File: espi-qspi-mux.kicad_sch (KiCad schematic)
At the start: 0 parts

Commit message: [#81876] Update date, Regroup OSM L block to make it interchangeable
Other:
- title: (none) -> BMC Reference Carrier Board
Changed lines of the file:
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@@
 	(generator_version "9.0")
 	(paper "A3")
+	(title_block
+		(title "BMC Reference Carrier Board")
+		(date "2025-08-14")
+		(rev "1.0.0")
+	)
 	(hierarchical_label "QSPI{QSPI}"
 		(shape bidirectional)

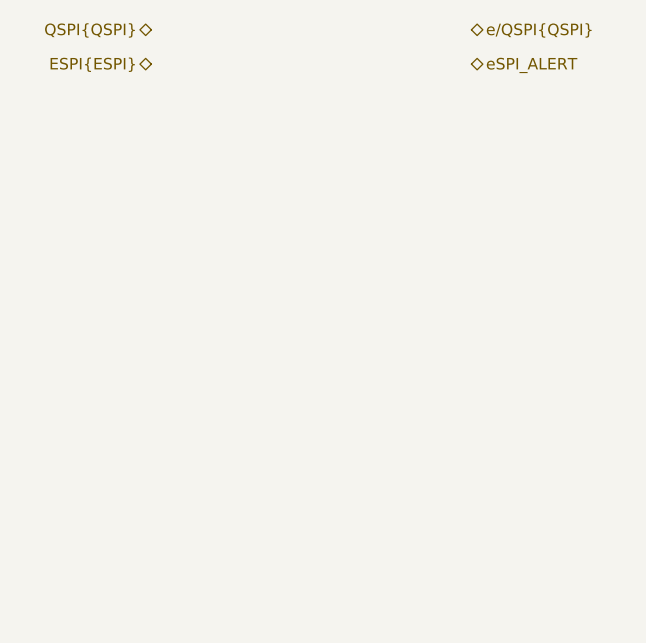
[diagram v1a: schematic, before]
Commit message: [#82233] Add eSPI/QSPI and TPM mux
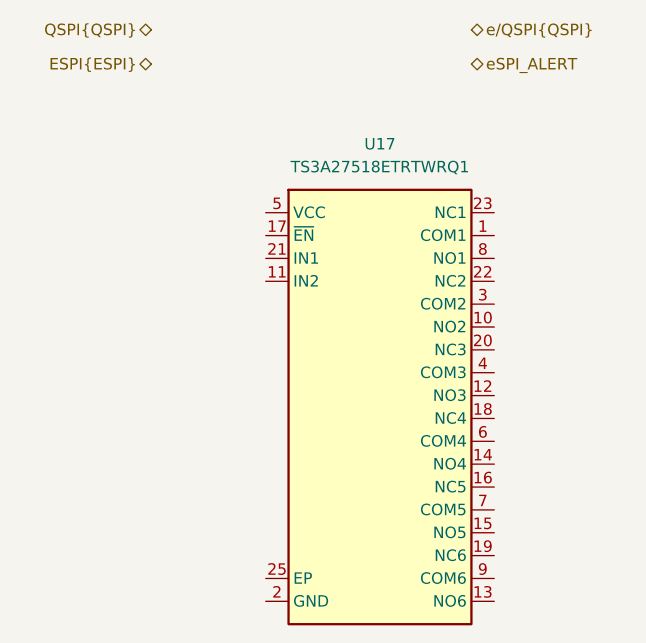
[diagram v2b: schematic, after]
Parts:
- added U17: TS3A27518E_QFN, antmicro-footprints:QFN-24-1EP_4x4mm_P0.5mm_EP2.6x2.6mm, symbol antmicroInterfaceAnalogSwitchesMultiplexersDemultiplexers:TS3A27518E_QFN
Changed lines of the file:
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@@
+		)
+	)
+	(symbol
+		(lib_id "antmicroInterfaceAnalogSwitchesMultiplexersDemultiplexers:TS3A27518E_QFN")
+		(at 153.67 149.86 0)
+		(unit 1)
+		(exclude_from_sim no)
+		(in_bom yes)
+		(on_board yes)
+		(dnp no)
+		(fields_autoplaced yes)
+		(property "Reference" "U17"
+			(at 166.37 142.24 0)
+			(effects
+				(font
+					(size 1.27 1.27)
+					(thickness 0.15)
+				)
+			)
+		)
+		(property "Value" "TS3A27518E_QFN"
+			(at 193.04 154.94 0)
+			(effects
+				(font
+					(size 1.27 1.27)
+					(thickness 0.15)
+				)
+				(justify left bottom)
+				(hide yes)
+			)
+		)
+		(property "Footprint" "antmicro-footprints:QFN-24-1EP_4x4mm_P0.5mm_EP2.6x2.6mm"
+			(at 193.04 157.48 0)
+			(effects
+				(font
+					(size 1.27 1.27)
+					(thickness 0.15)
+				)
+				(justify left bottom)
+				(hide yes)
+			)
+		)
+		(property "Datasheet" "https://www.ti.com/lit/ds/symlink/ts3a27518e-q1.pdf?HQS=dis-mous-null-mousermode-dsf-pf-null-wwe&ts=1685014732392&ref_url=https%253A%252F%252Fwww.mouser.com%252F"
+			(at 193.04 160.02 0)
+			(effects
+				(font
+					(size 1.27 1.27)
+					(thickness 0.15)
+				)
+				(justify left bottom)
+				(hide yes)
+			)
+		)
+		(property "Description" "Interface analog switch/multiplexer/demultiplexer"
+			(at 153.67 149.86 0)
+			(effects
+				(font
+					(size 1.27 1.27)
+				)
+				(hide yes)
+			)
+		)
+		(property "MPN" "TS3A27518ETRTWRQ1"
+			(at 166.37 144.78 0)
+			(effects
+				(font
+					(size 1.27 1.27)
+					(thickness 0.15)
+				)
+			)
+		)
+		(property "Manufacturer" "Texas Instruments"
+			(at 193.04 165.1 0)
+			(effects
+				(font
+					(size 1.27 1.27)
+					(thickness 0.15)
+				)
+				(justify left bottom)
+				(hide yes)
+			)
+		)
+		(property "Author" "Antmicro"
+			(at 193.04 167.64 0)
+			(effects
+				(font
+					(size 1.27 1.27)
+					(thickness 0.15)
+				)
+				(justify left bottom)
+				(hide yes)
+			)
+		)
+		(property "License" "Apache-2.0"
+			(at 193.04 170.18 0)
+			(effects
+				(font
+					(size 1.27 1.27)
+					(thickness 0.15)
+				)
+				(justify left bottom)
+				(hide yes)
+			)
+		)
+		(pin "4"
+		)
+		(pin "1"
+		)
+		(pin "7"
+		)
+		(pin "16"
+		)
+		(pin "24"
+		)
+		(pin "25"
+		)
+		(pin "13"
+		)
+		(pin "9"
+		)
+		(pin "18"
+		)
+		(pin "6"
+		)
+		(pin "8"
+		)
+		(pin "20"
+		)
+		(pin "10"
+		)
+		(pin "23"
+		)
+		(pin "3"
+		)
+		(pin "14"
+		)
+		(pin "12"
+		)
+		(pin "15"
+		)
+		(pin "21"
+		)
+		(pin "11"
+		)
+		(pin "5"
+		)
+		(pin "22"
+		)
+		(pin "2"
+		)
+		(pin "17"
+		)
+		(pin "19"
+		)
+		(instances
+			(project ""
+				(path "/5f636c45-3c15-4731-8931-4625e0dab7e4/e532ae7c-55b4-427b-a317-9e407e1b3e94"
+					(reference "U17")
+					(unit 1)
+				)
+			)
 		)
 	)

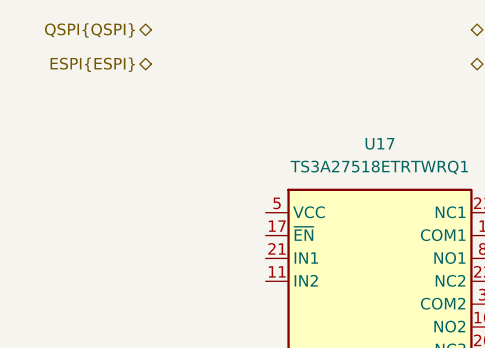
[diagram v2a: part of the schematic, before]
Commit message: [#82323] ESPI -> eSPI
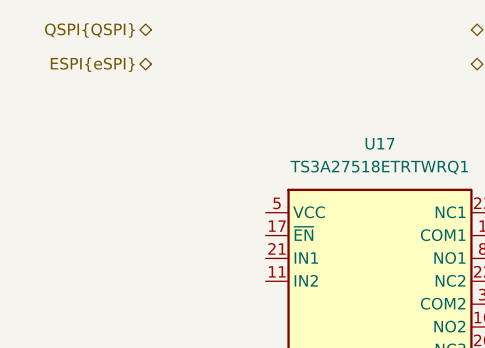
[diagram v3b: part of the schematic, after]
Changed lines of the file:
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@@
 		)
 	)
-	(hierarchical_label "ESPI{ESPI}"
+	(hierarchical_label "ESPI{eSPI}"
 		(shape bidirectional)
 		(at 140.97 133.35 180)

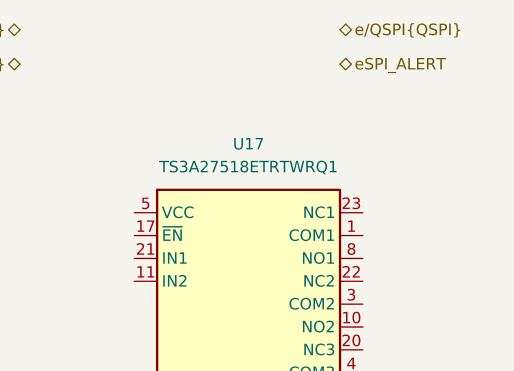
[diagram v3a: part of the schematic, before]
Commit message: [#82323] Connect OSM signals
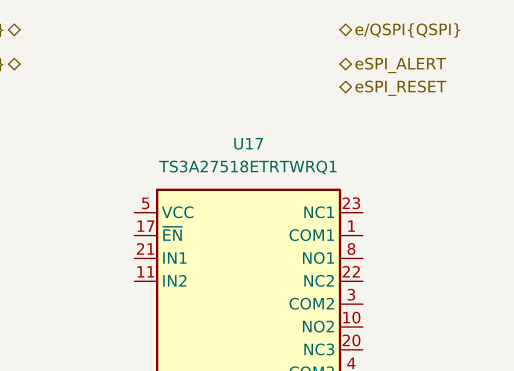
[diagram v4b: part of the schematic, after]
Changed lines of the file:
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@@
+		)
+	)
+	(hierarchical_label "eSPI_RESET"
+		(shape bidirectional)
+		(at 176.53 135.89 0)
+		(effects
+			(font
+				(size 1.27 1.27)
+			)
+			(justify left)
 		)
 	)

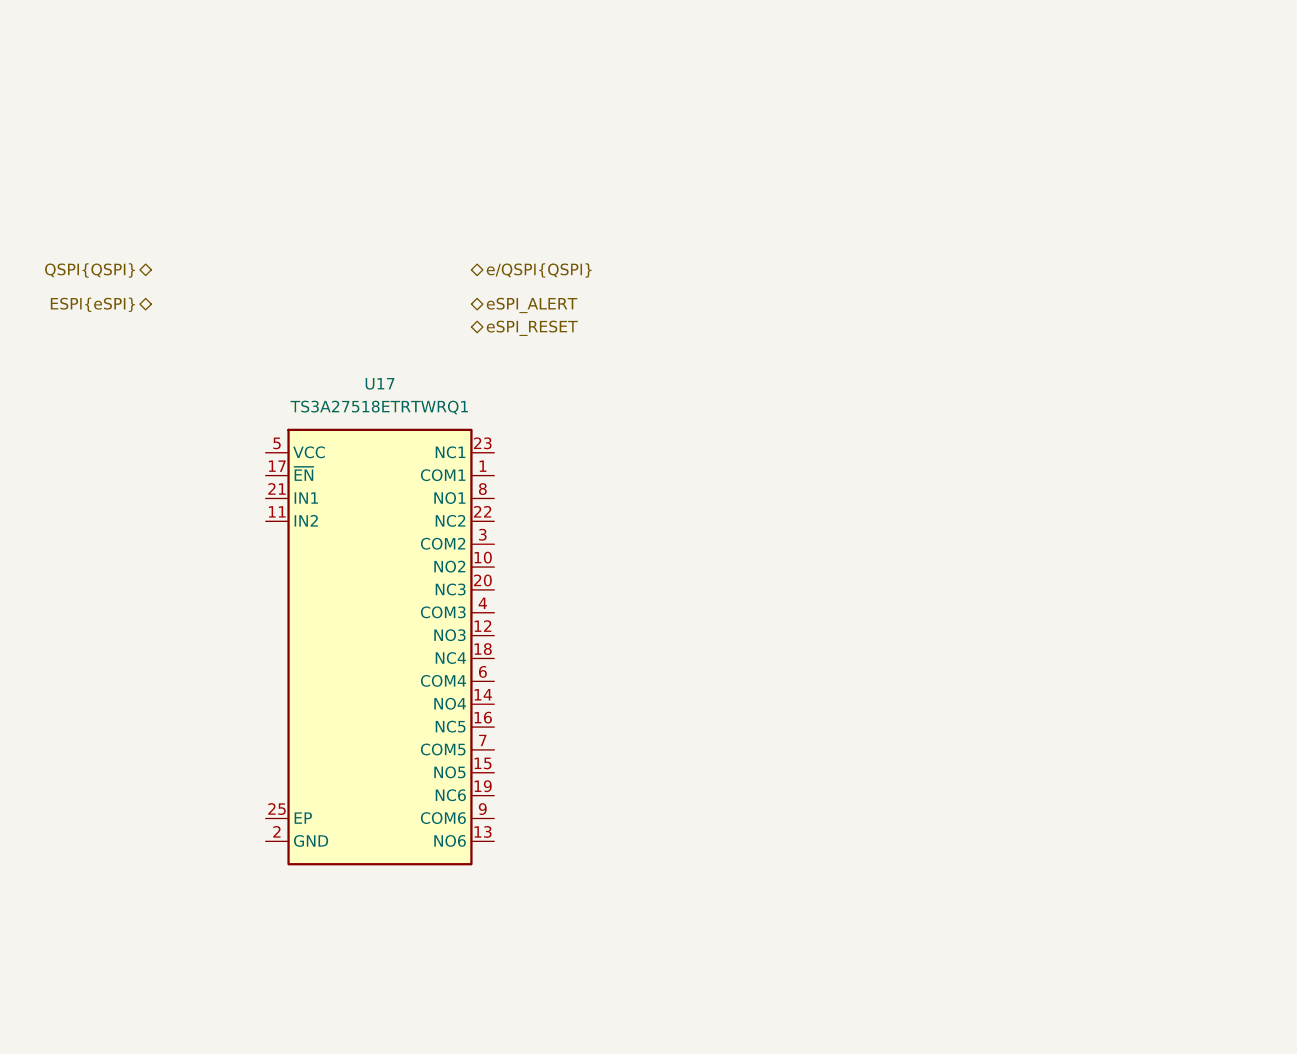
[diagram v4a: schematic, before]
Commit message: [#82233] Added eSPI/QSPI mux and DNP QSPI flash memory
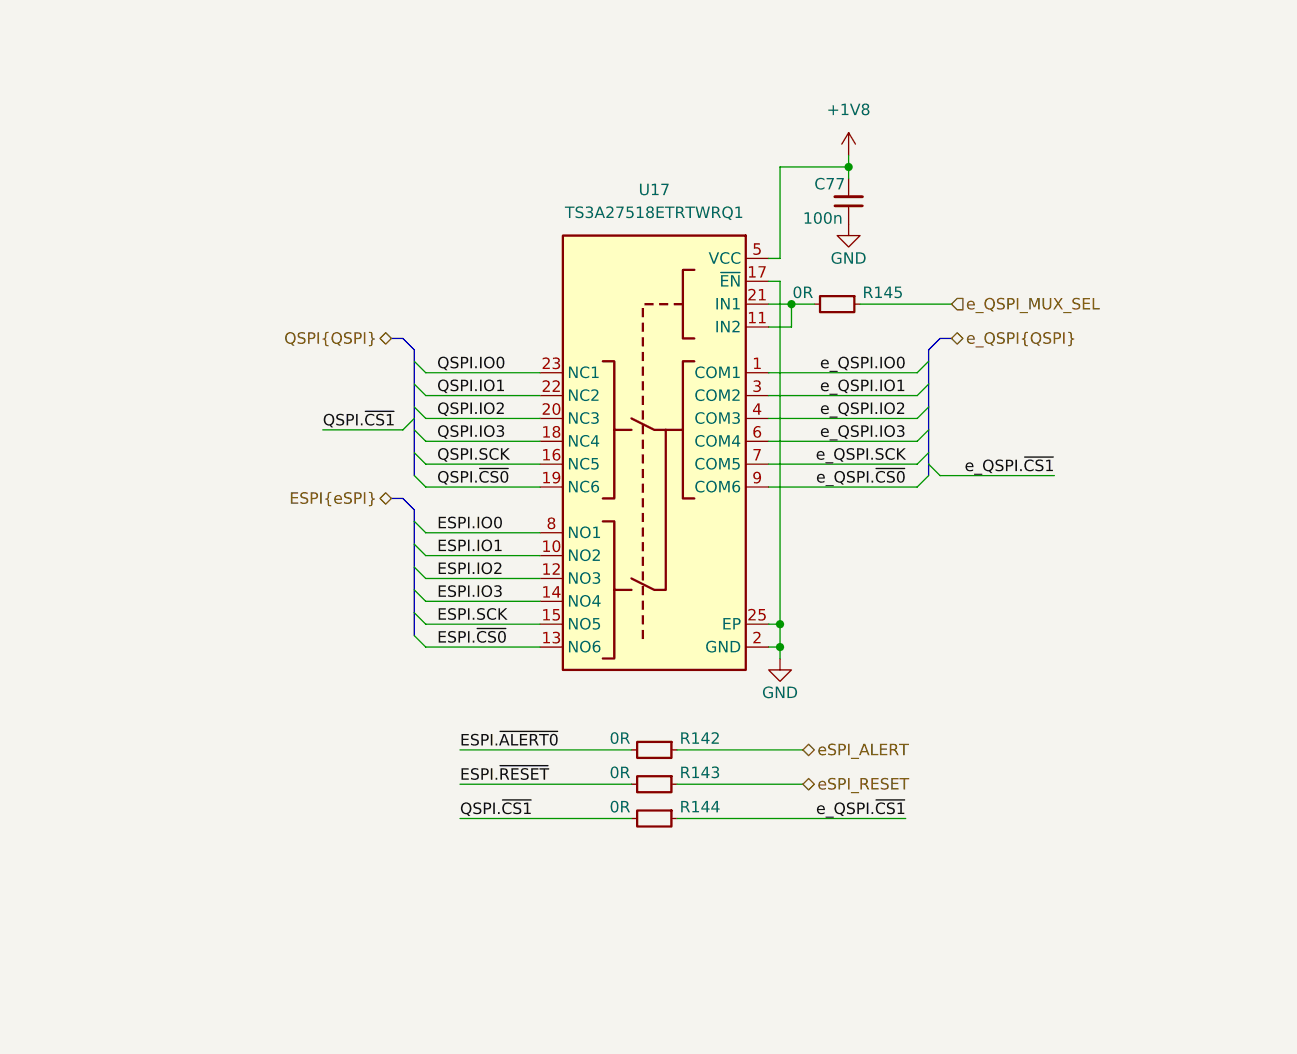
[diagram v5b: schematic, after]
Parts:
- added C77: C_100n_0402, antmicro-footprints:C_0402_1005Metric, symbol antmicroCapacitors0402:C_100n_0402
- added R142, R143, R144, R145: R_0R_0402, antmicro-footprints:R_0402_1005Metric, symbol antmicroResistors0402:R_0R_0402
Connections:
- net eSPI_ALERT: now also R142.1
- net eSPI_RESET: now also R143.1
- net e_QSPI.IO0: now reaches U17.1 (COM1)
- net ESPI.IO1: now reaches U17.10 (NO2)
- net at U17.11 (IN2): now also U17.21 (IN1), R145.2
- net ESPI.IO2: now reaches U17.12 (NO3)
- net ESPI.~{CS0}: now reaches U17.13 (NO6)
- net ESPI.IO3: now reaches U17.14 (NO4)
- net ESPI.SCK: now reaches U17.15 (NO5)
- net QSPI.SCK: now reaches U17.16 (NC5)
- net GND: now reaches U17.17 (~{EN})
- net GND: now also U17.2 (GND), U17.25 (EP), C77.1
- net QSPI.IO3: now reaches U17.18 (NC4)
- net QSPI.~{CS0}: now reaches U17.19 (NC6)
- net QSPI.IO2: now reaches U17.20 (NC3)
- net QSPI.IO1: now reaches U17.22 (NC2)
- net QSPI.IO0: now reaches U17.23 (NC1)
- net e_QSPI.IO1: now reaches U17.3 (COM2)
- net e_QSPI.IO2: now reaches U17.4 (COM3)
- net +1V8: now reaches U17.5 (VCC)
- net +1V8: now also C77.2
- net e_QSPI.IO3: now reaches U17.6 (COM4)
- net e_QSPI.SCK: now reaches U17.7 (COM5)
- net ESPI.IO0: now reaches U17.8 (NO1)
- net e_QSPI.~{CS0}: now reaches U17.9 (COM6)
- new net ESPI.~{ALERT0}: R142.2
- new net ESPI.~{RESET}: R143.2
- new net QSPI.~{CS1}: R144.2
- new net e_QSPI.~{CS1}: R144.1
- new net e_QSPI_MUX_SEL: R145.1

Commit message: Changed A4 sheets to A3 and cleaned them up
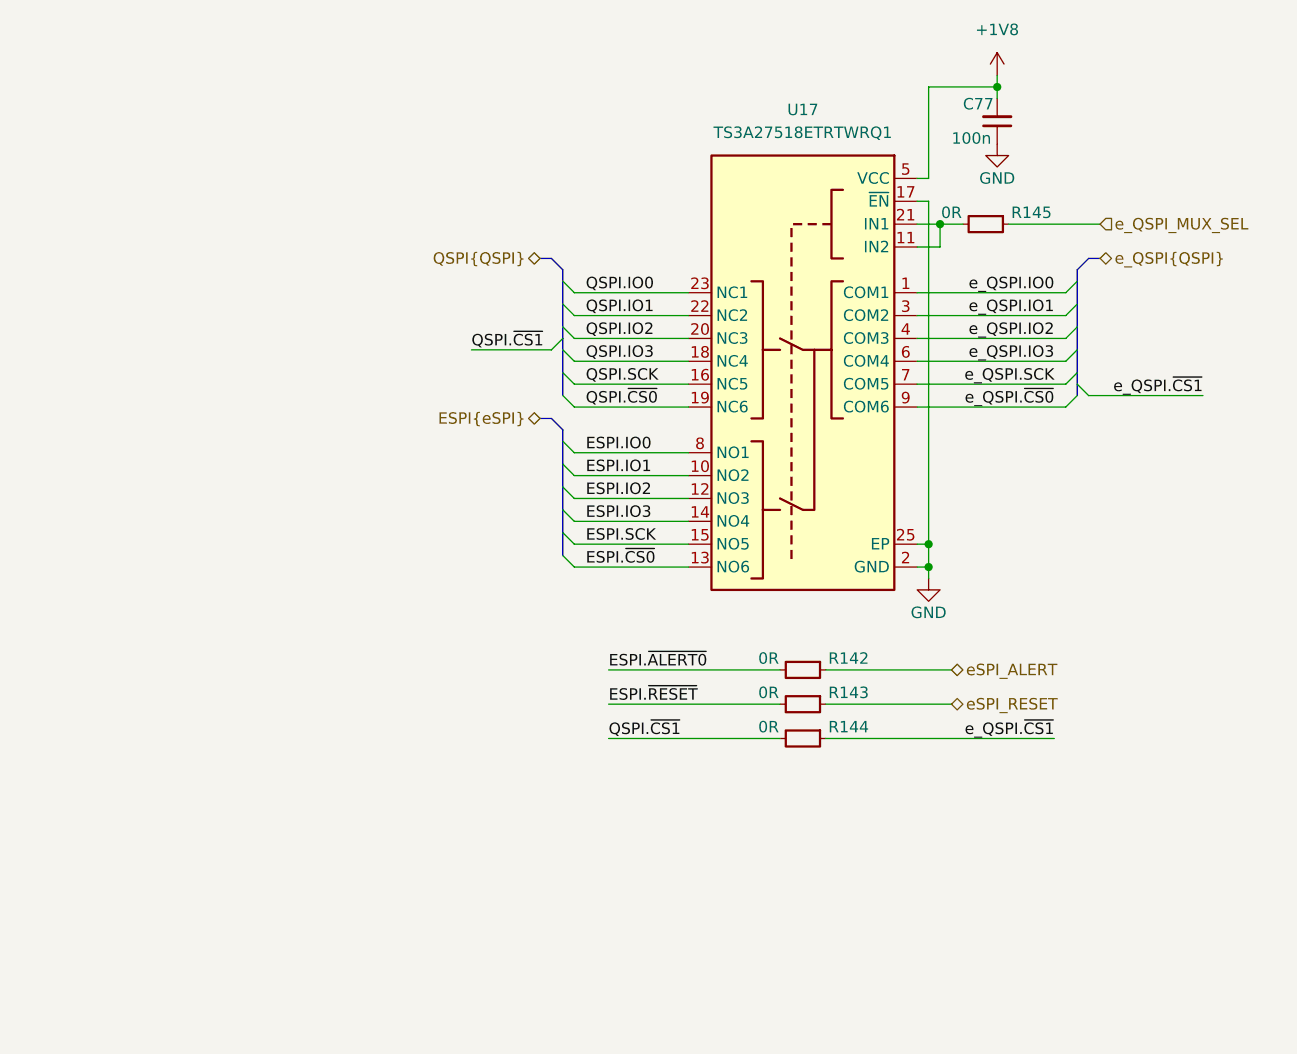
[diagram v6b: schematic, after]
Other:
- moved on the sheet: C77, R142, R143, R144, R145, U17

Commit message: [#83336] Small front panel interface fixes
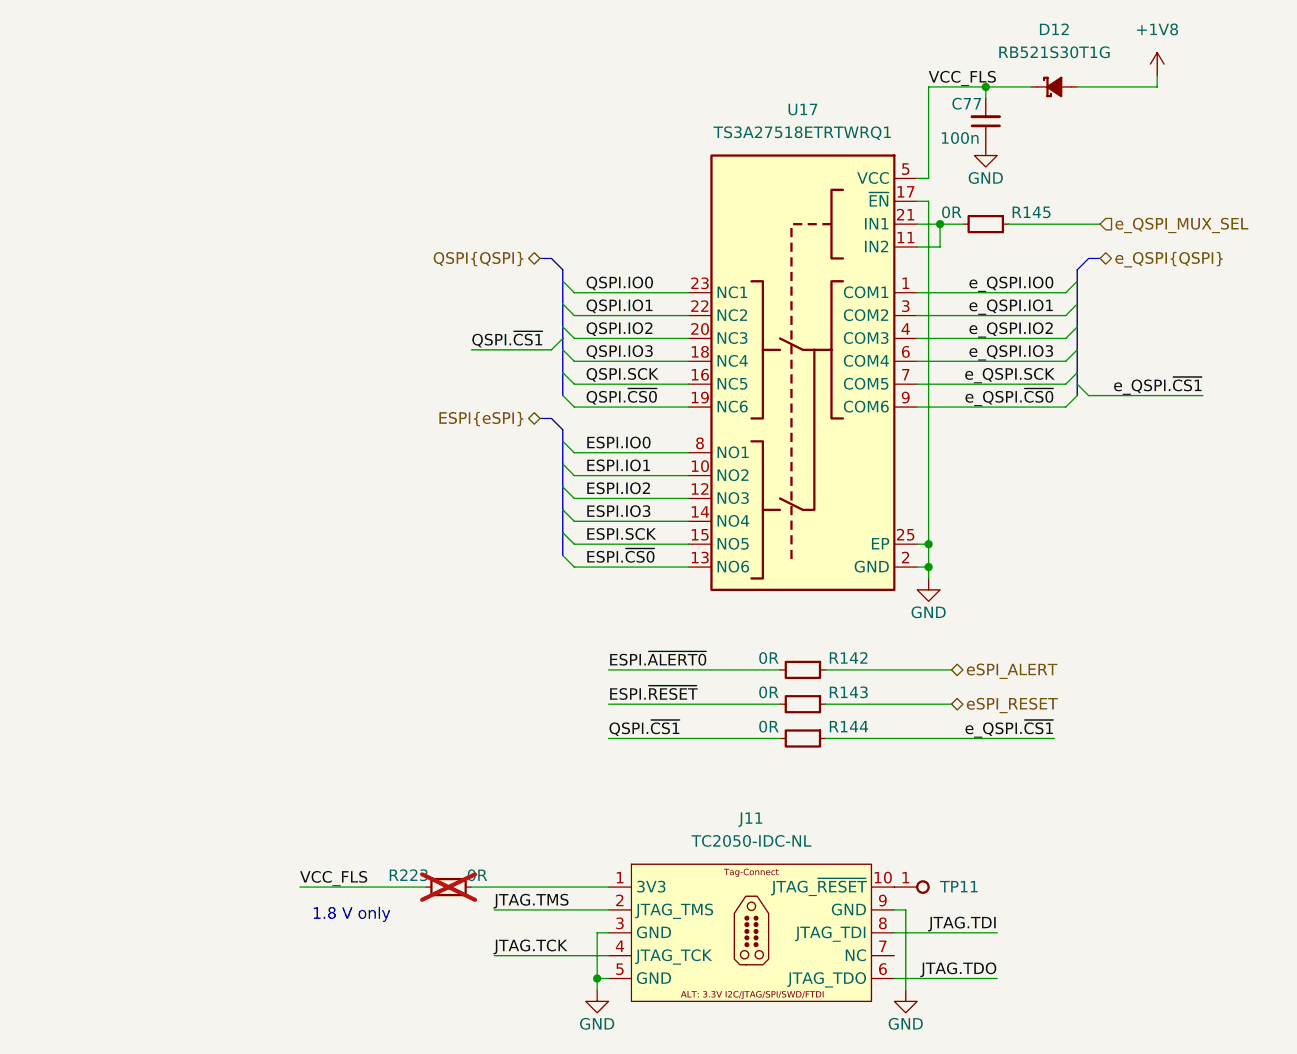
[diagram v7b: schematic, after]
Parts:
- added D12: RB521S30T1G, antmicro-footprints:SOD-523, symbol antmicroDiodesRectifiersSingle:RB521S30T1G
- added J11: Tag-Connect_TC2050-IDC-NL_2x5_P1.27mm, antmicro-footprints:Tag-Connect_TC2050-IDC-NL_2x5_P1.27mm, symbol antmicroTestPoints:Tag-Connect_TC2050-IDC-NL_2x5_P1.27mm
- added R223: R_0R_0402, antmicro-footprints:R_0402_1005Metric, symbol antmicroResistors0402:R_0R_0402
- added TP11: TP_0.75mm_SMD, antmicro-footprints:TP_SMD_0.75mm, symbol antmicroTestPoints:TP_0.75mm_SMD
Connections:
- net +1V8: now also D12.2 (A); no longer C77.2, U17.5 (VCC)
- net GND: now also J11.3, J11.5, J11.9
- new net: J11.1, R223.2
- new net: J11.10, TP11.1
- new net JTAG.TCK: J11.4
- new net JTAG.TDI: J11.8
- new net JTAG.TDO: J11.6
- new net JTAG.TMS: J11.2
- new net VCC_FLS: C77.2, D12.1 (C), R223.1, U17.5 (VCC)
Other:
- note added: "1.8 V only"
- moved on the sheet: C77
